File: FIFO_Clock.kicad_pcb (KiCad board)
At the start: 2 copper layers, 100 x 100 mm, 52 parts, among them J1 U262-16XN-4BVC11, J2 AVR-ISP-6, SW1 SKHMQKE010, SW2 SW_5_Way, U1 ATtiny84A-SSUR, U2 DS1307Z+, Y1 32.768 kHz

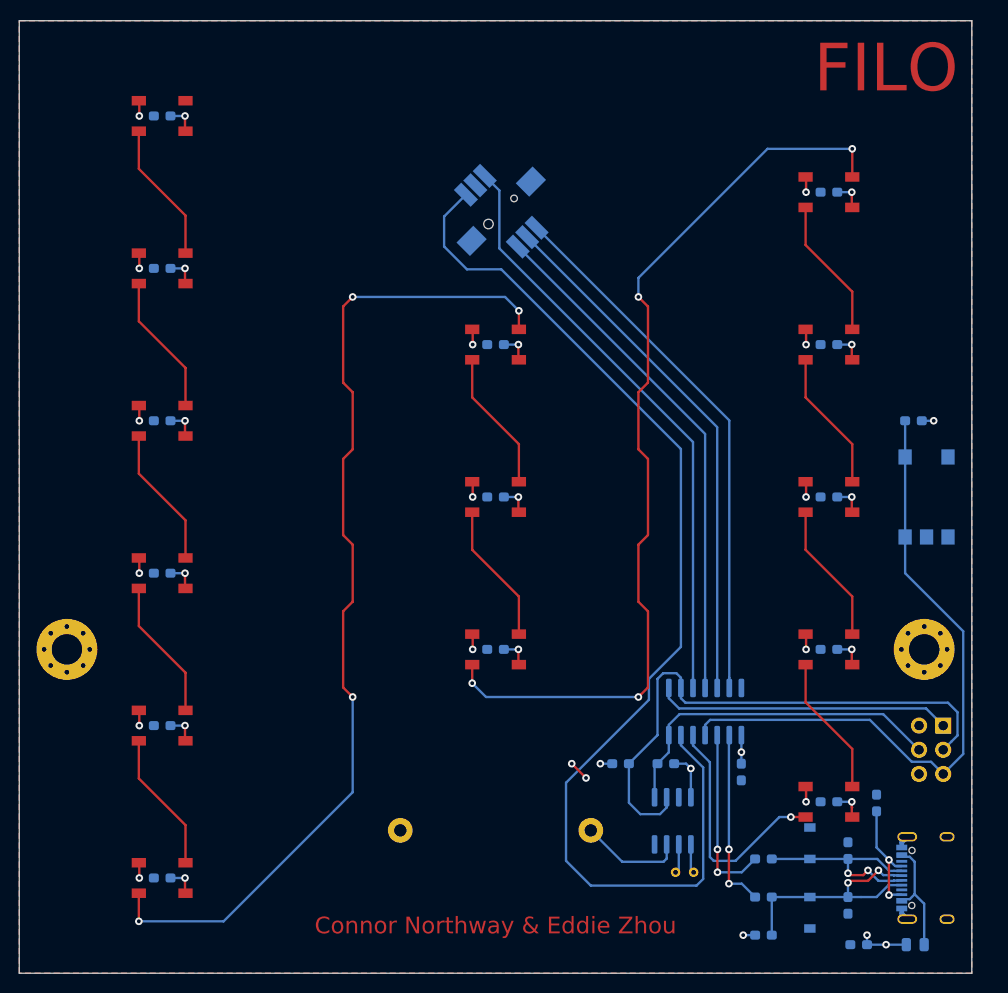
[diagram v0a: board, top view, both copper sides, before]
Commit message: v1.1 changes transferred, FILO->FIFO change
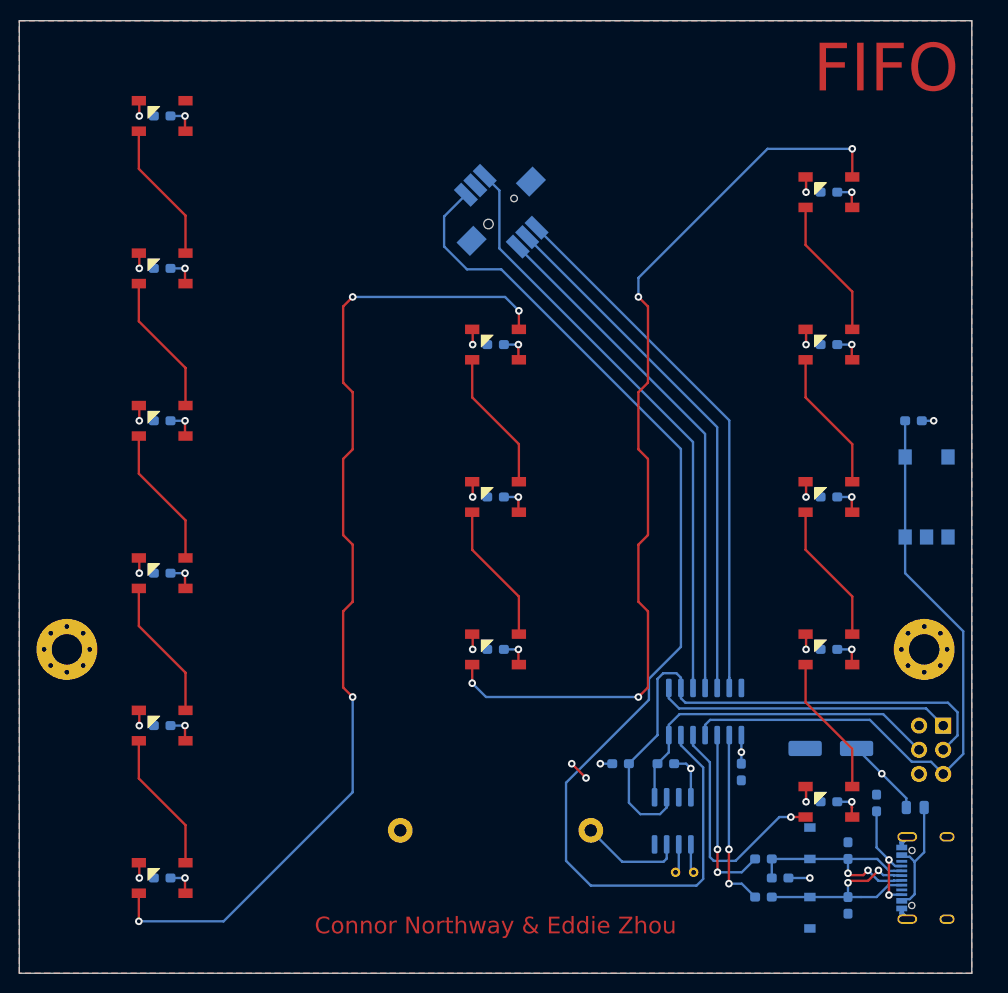
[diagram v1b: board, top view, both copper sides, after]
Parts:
- C2: footprint Capacitor_SMD:C_0603_1608Metric_Pad1.05x0.95mm_HandSolder -> Capacitor_SMD:CP_Elec_6.3x5.8
- moved C2 20.8 mm to (135.2, 126.4)
- moved F1 14.4 mm to (144.1, 132.6)
- moved R1 6.25 mm to (129.9, 140.0), turned to 180 degrees
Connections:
- R1 pad 2: Net-(D2-Pad1) -> Net-(D1-Pad1)
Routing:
- net +5V: track 60.9 -> 65.1 mm, vias 21 -> 20
- net Net-(D2-Pad1): track 26.1 -> 22.1 mm
- net Net-(D1-Pad1): track 22.1 -> 23.9 mm
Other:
- board text added: "FIFO"
- board text added: "FIFO Clock v1.1"
- board text removed: "FILO"
- board text removed: "FILO Clock v1.0"

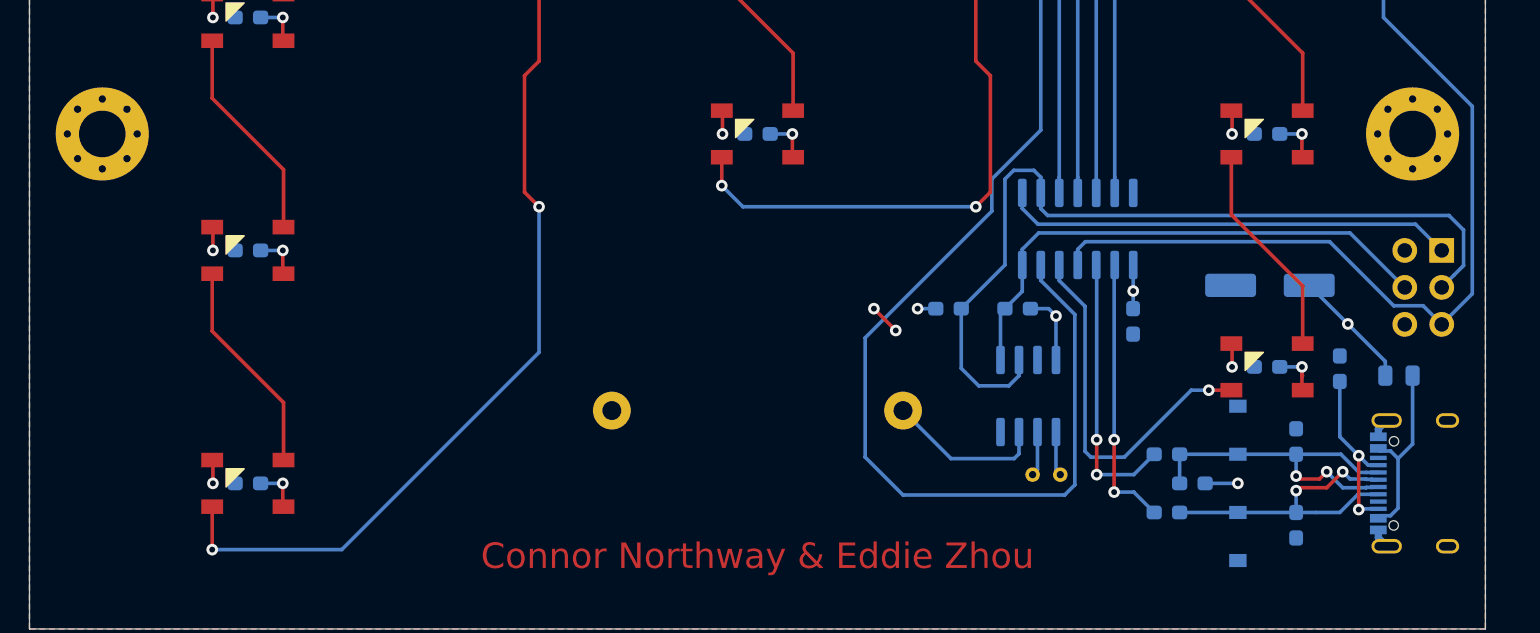
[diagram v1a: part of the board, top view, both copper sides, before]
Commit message: Fix usb CC pulldown circuit
make sure to use two pulldown resistors instead of shorting CC lines
found this while trying to repurpose one of the old pcbs for something else

<x> years later I have a slightly better understanding of the USB spec..
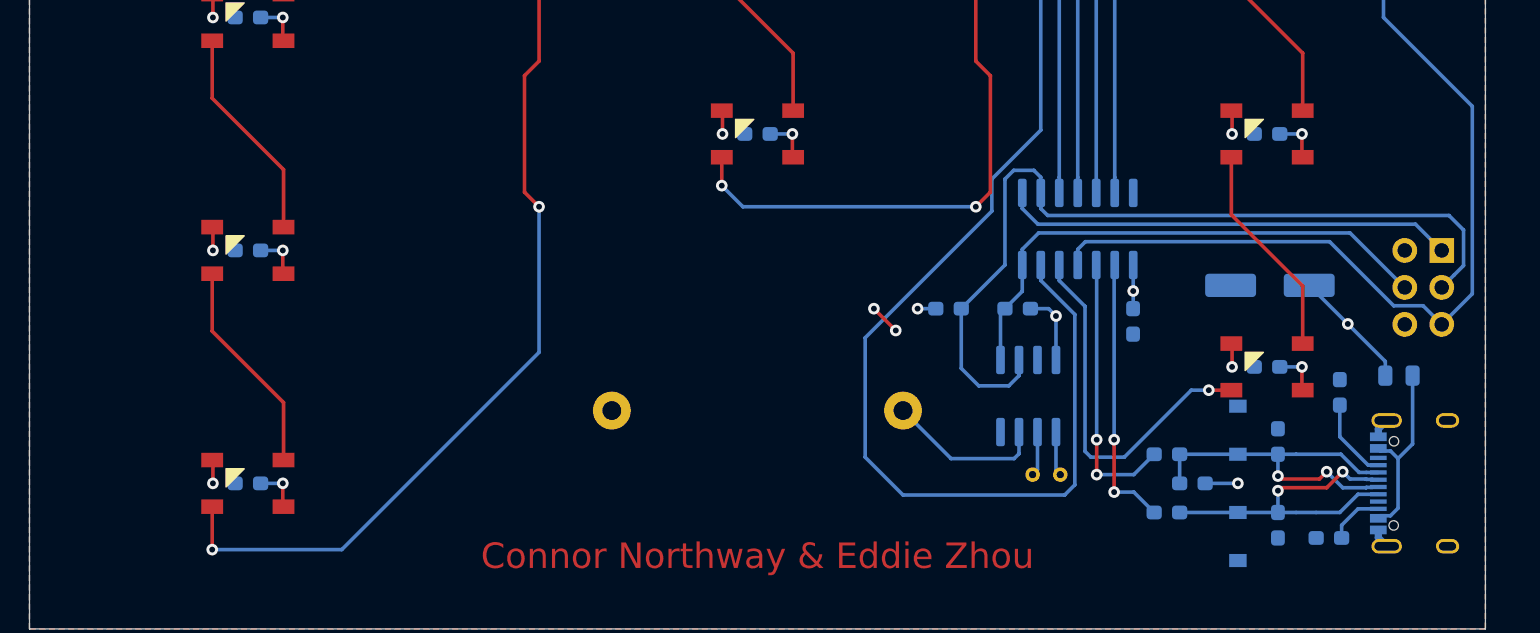
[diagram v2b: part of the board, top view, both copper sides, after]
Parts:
- removed REF** (x2): MountingHole_3.2mm_M3_Pad_Via, MountingHole:MountingHole_3.2mm_M3_Pad_Via
- added R7: 5.1k, Resistor_SMD:R_0603_1608Metric_Pad1.05x0.95mm_HandSolder, B.Cu at (139.2, 143.8)
- moved R8 1.62 mm to (140.0, 133.8)
- moved RV1 1.25 mm to (135.8, 142.9)
- moved RV2 1.25 mm to (135.8, 137.1)
- renumbered R7 to R8
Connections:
- D3 pad 4: Net-(D3-Pad4) -> unconnected-(D3-Pad4)
- J1 pad A8: Net-(J1-PadA8) -> unconnected-(J1-PadA8)
- J1 pad B5: Net-(J1-PadA5) -> Net-(J1-PadB5)
- J1 pad B8: Net-(J1-PadB8) -> unconnected-(J1-PadB8)
- U2 pad 7: Net-(U2-Pad7) -> unconnected-(U2-Pad7)
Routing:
- net Net-(J1-PadA5): track 12.3 -> 5.63 mm, vias 2 -> 0
- net Net-(J1-PadB5): track 0.00 -> 3.86 mm
- net Net-(D1-Pad1): track 23.9 -> 25.1 mm
- net Net-(D2-Pad1): track 22.1 -> 23.3 mm
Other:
- net class Default removed
